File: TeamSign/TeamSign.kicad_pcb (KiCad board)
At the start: 2 copper layers, 0 parts

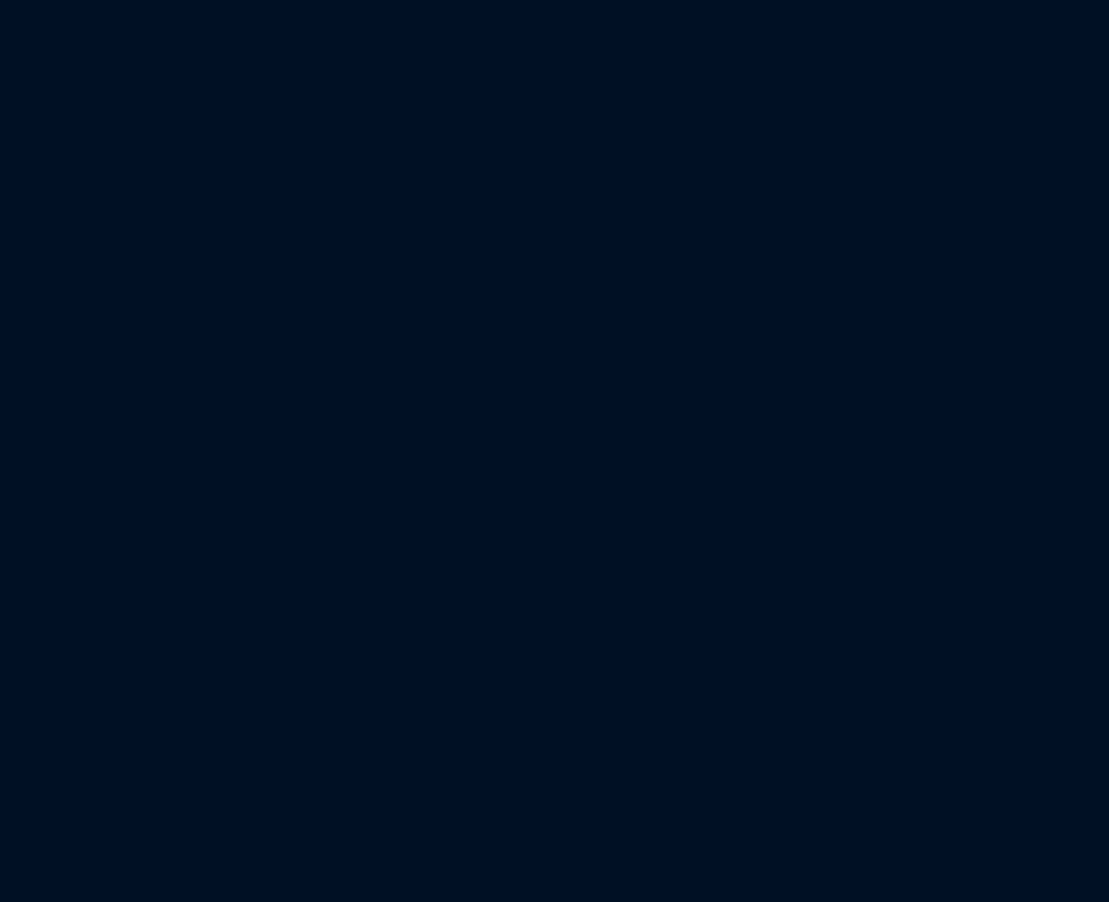
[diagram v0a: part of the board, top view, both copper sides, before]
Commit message: Add SK6812-Side-A footprint/symbol to working area, as well as swapped to a stacklight connection that has a ground pin at the end for generic 12v power use.  yay!
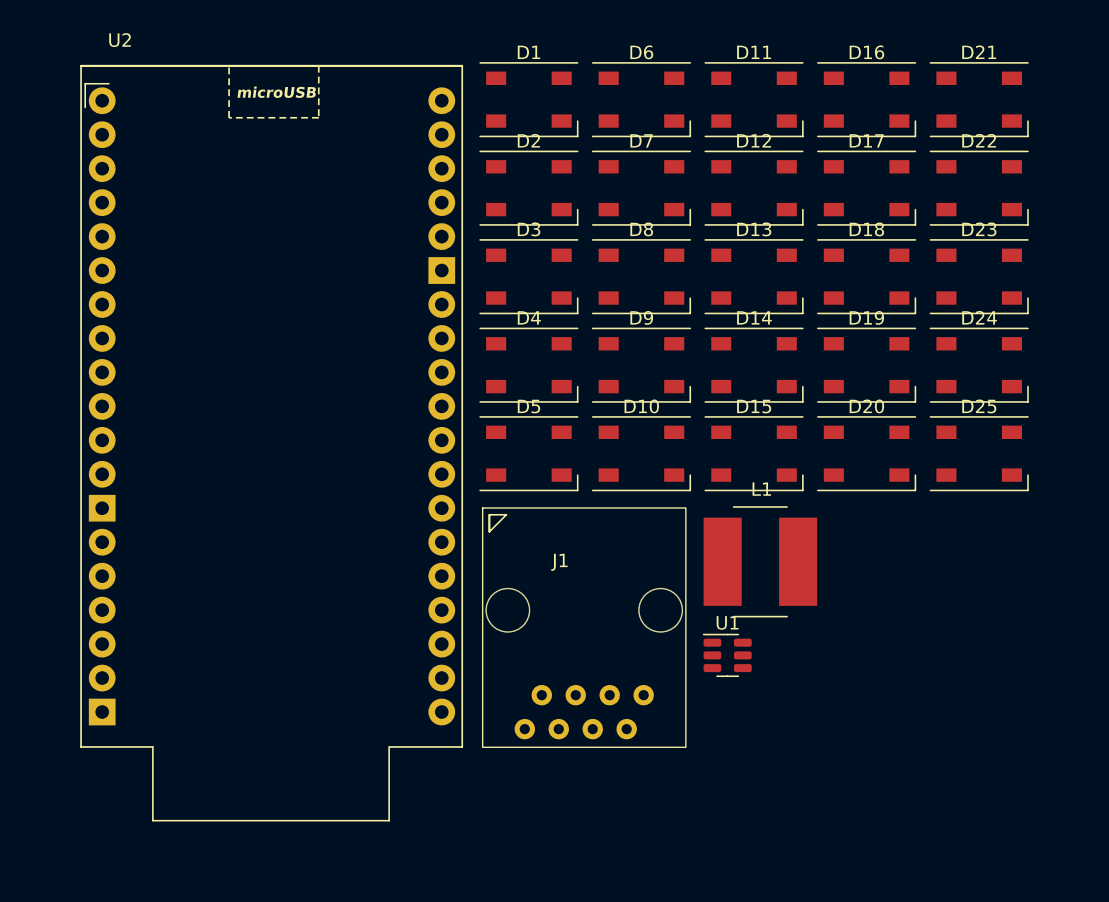
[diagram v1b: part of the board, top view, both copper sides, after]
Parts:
- added D1: SK6812, LED_SMD:LED_SK6812_PLCC4_5.0x5.0mm_P3.2mm, F.Cu at (108.5, -45.9)
- added D10: SK6812, LED_SMD:LED_SK6812_PLCC4_5.0x5.0mm_P3.2mm, F.Cu at (116.9, -19.4)
- added D11: SK6812, LED_SMD:LED_SK6812_PLCC4_5.0x5.0mm_P3.2mm, F.Cu at (125.3, -45.9)
- added D12: SK6812, LED_SMD:LED_SK6812_PLCC4_5.0x5.0mm_P3.2mm, F.Cu at (125.3, -39.3)
- added D13: SK6812, LED_SMD:LED_SK6812_PLCC4_5.0x5.0mm_P3.2mm, F.Cu at (125.3, -32.7)
- added D14: SK6812, LED_SMD:LED_SK6812_PLCC4_5.0x5.0mm_P3.2mm, F.Cu at (125.3, -26.1)
- added D15: SK6812, LED_SMD:LED_SK6812_PLCC4_5.0x5.0mm_P3.2mm, F.Cu at (125.3, -19.4)
- added D16: SK6812, LED_SMD:LED_SK6812_PLCC4_5.0x5.0mm_P3.2mm, F.Cu at (133.8, -45.9)
- added D17: SK6812, LED_SMD:LED_SK6812_PLCC4_5.0x5.0mm_P3.2mm, F.Cu at (133.8, -39.3)
- added D18: SK6812, LED_SMD:LED_SK6812_PLCC4_5.0x5.0mm_P3.2mm, F.Cu at (133.8, -32.7)
- added D19: SK6812, LED_SMD:LED_SK6812_PLCC4_5.0x5.0mm_P3.2mm, F.Cu at (133.8, -26.1)
- added D2: SK6812, LED_SMD:LED_SK6812_PLCC4_5.0x5.0mm_P3.2mm, F.Cu at (108.5, -39.3)
- added D20: SK6812, LED_SMD:LED_SK6812_PLCC4_5.0x5.0mm_P3.2mm, F.Cu at (133.8, -19.4)
- added D21: SK6812, LED_SMD:LED_SK6812_PLCC4_5.0x5.0mm_P3.2mm, F.Cu at (142.2, -45.9)
- added D22: SK6812, LED_SMD:LED_SK6812_PLCC4_5.0x5.0mm_P3.2mm, F.Cu at (142.2, -39.3)
- added D23: SK6812, LED_SMD:LED_SK6812_PLCC4_5.0x5.0mm_P3.2mm, F.Cu at (142.2, -32.7)
- added D24: SK6812, LED_SMD:LED_SK6812_PLCC4_5.0x5.0mm_P3.2mm, F.Cu at (142.2, -26.1)
- added D25: SK6812, LED_SMD:LED_SK6812_PLCC4_5.0x5.0mm_P3.2mm, F.Cu at (142.2, -19.4)
- added D3: SK6812, LED_SMD:LED_SK6812_PLCC4_5.0x5.0mm_P3.2mm, F.Cu at (108.5, -32.7)
- added D4: SK6812, LED_SMD:LED_SK6812_PLCC4_5.0x5.0mm_P3.2mm, F.Cu at (108.5, -26.1)
- added D5: SK6812, LED_SMD:LED_SK6812_PLCC4_5.0x5.0mm_P3.2mm, F.Cu at (108.5, -19.4)
- added D6: SK6812, LED_SMD:LED_SK6812_PLCC4_5.0x5.0mm_P3.2mm, F.Cu at (116.9, -45.9)
- added D7: SK6812, LED_SMD:LED_SK6812_PLCC4_5.0x5.0mm_P3.2mm, F.Cu at (116.9, -39.3)
- added D8: SK6812, LED_SMD:LED_SK6812_PLCC4_5.0x5.0mm_P3.2mm, F.Cu at (116.9, -32.7)
- added D9: SK6812, LED_SMD:LED_SK6812_PLCC4_5.0x5.0mm_P3.2mm, F.Cu at (116.9, -26.1)
- added J1: RJ45, footprints:RCH RC00139, F.Cu at (105.0, -15.4)
- added L1: 3.3uH, Inductor_SMD:L_Bourns_SRN8040TA, F.Cu at (125.8, -11.4)
- added U1: TPS563200, Package_TO_SOT_SMD:SOT-23-6, F.Cu at (123.4, -4.36)
- added U2: ESP32-Devkit_C_V4, footprints:MODULE_ESP32_DEVKIT_C_V4, F.Cu at (89.3, -23.0)
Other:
- board outline added: 14.7 x 3.2 mm

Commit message: Added subsheet for the other LEDs, still need to fix the capacitor footprint, but making solid progress it seems?  Wild!
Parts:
- added D26: SK6812-Side-A, footprints:SK6812-Side-A, F.Cu at (37.8, 56.2)
- added D27: SK6812-Side-A, footprints:SK6812-Side-A, F.Cu at (37.7, 66.3)
- added D28: SK6812-Side-A, footprints:SK6812-Side-A, F.Cu at (36.5, 78.5)
- added D29: SK6812-Side-A, footprints:SK6812-Side-A, F.Cu at (36.4, 88.9)
- added D30: SK6812-Side-A, footprints:SK6812-Side-A, F.Cu at (36.5, 99.5)
- added D31: SK6812-Side-A, footprints:SK6812-Side-A, F.Cu at (35.6, 113.6)
- added D32: SK6812-Side-A, footprints:SK6812-Side-A, F.Cu at (35.5, 125.9)
- added D33: SK6812-Side-A, footprints:SK6812-Side-A, F.Cu at (35.9, 141.9)
- added D34: SK6812, LED_SMD:LED_SK6812_PLCC4_5.0x5.0mm_P3.2mm, F.Cu at (67.2, 100.2)
- added D35: SK6812, LED_SMD:LED_SK6812_PLCC4_5.0x5.0mm_P3.2mm, F.Cu at (73.8, 100.2)
- added D36: SK6812, LED_SMD:LED_SK6812_PLCC4_5.0x5.0mm_P3.2mm, F.Cu at (80.4, 100.2)
- added D37: SK6812, LED_SMD:LED_SK6812_PLCC4_5.0x5.0mm_P3.2mm, F.Cu at (149.6, -11.7)
- added D38: SK6812, LED_SMD:LED_SK6812_PLCC4_5.0x5.0mm_P3.2mm, F.Cu at (149.6, -5.03)
- added D39: SK6812, LED_SMD:LED_SK6812_PLCC4_5.0x5.0mm_P3.2mm, F.Cu at (149.6, 1.59)
- added D40: SK6812, LED_SMD:LED_SK6812_PLCC4_5.0x5.0mm_P3.2mm, F.Cu at (149.6, 8.21)
- added D41: SK6812, LED_SMD:LED_SK6812_PLCC4_5.0x5.0mm_P3.2mm, F.Cu at (149.6, 14.8)
- added D42: SK6812, LED_SMD:LED_SK6812_PLCC4_5.0x5.0mm_P3.2mm, F.Cu at (149.6, 21.4)
- added D43: SK6812, LED_SMD:LED_SK6812_PLCC4_5.0x5.0mm_P3.2mm, F.Cu at (149.6, 28.1)
- added D44: SK6812, LED_SMD:LED_SK6812_PLCC4_5.0x5.0mm_P3.2mm, F.Cu at (158.0, -11.7)
- added D45: SK6812, LED_SMD:LED_SK6812_PLCC4_5.0x5.0mm_P3.2mm, F.Cu at (158.0, -5.03)
- added D46: SK6812, LED_SMD:LED_SK6812_PLCC4_5.0x5.0mm_P3.2mm, F.Cu at (158.0, 1.59)
- added D47: SK6812, LED_SMD:LED_SK6812_PLCC4_5.0x5.0mm_P3.2mm, F.Cu at (158.0, 8.21)
- added D48: SK6812, LED_SMD:LED_SK6812_PLCC4_5.0x5.0mm_P3.2mm, F.Cu at (158.0, 14.8)
- added D49: SK6812, LED_SMD:LED_SK6812_PLCC4_5.0x5.0mm_P3.2mm, F.Cu at (158.0, 21.4)
- added D50: SK6812, LED_SMD:LED_SK6812_PLCC4_5.0x5.0mm_P3.2mm, F.Cu at (158.0, 28.1)
- added D51: SK6812, LED_SMD:LED_SK6812_PLCC4_5.0x5.0mm_P3.2mm, F.Cu at (166.4, -11.7)
- added D52: SK6812, LED_SMD:LED_SK6812_PLCC4_5.0x5.0mm_P3.2mm, F.Cu at (166.4, -5.03)
- added D53: SK6812, LED_SMD:LED_SK6812_PLCC4_5.0x5.0mm_P3.2mm, F.Cu at (166.4, 1.59)
- added D54: SK6812, LED_SMD:LED_SK6812_PLCC4_5.0x5.0mm_P3.2mm, F.Cu at (166.4, 8.21)
- added D55: SK6812, LED_SMD:LED_SK6812_PLCC4_5.0x5.0mm_P3.2mm, F.Cu at (166.4, 14.8)
- added D56: SK6812, LED_SMD:LED_SK6812_PLCC4_5.0x5.0mm_P3.2mm, F.Cu at (166.4, 21.4)
- added D57: SK6812, LED_SMD:LED_SK6812_PLCC4_5.0x5.0mm_P3.2mm, F.Cu at (166.4, 28.1)
- added D58: SK6812, LED_SMD:LED_SK6812_PLCC4_5.0x5.0mm_P3.2mm, F.Cu at (174.8, -11.7)
- added D59: SK6812, LED_SMD:LED_SK6812_PLCC4_5.0x5.0mm_P3.2mm, F.Cu at (174.8, -5.03)
- added D60: SK6812, LED_SMD:LED_SK6812_PLCC4_5.0x5.0mm_P3.2mm, F.Cu at (174.8, 1.59)
- added D61: SK6812, LED_SMD:LED_SK6812_PLCC4_5.0x5.0mm_P3.2mm, F.Cu at (174.8, 8.21)
- added D62: SK6812, LED_SMD:LED_SK6812_PLCC4_5.0x5.0mm_P3.2mm, F.Cu at (174.8, 14.8)
- added D63: SK6812, LED_SMD:LED_SK6812_PLCC4_5.0x5.0mm_P3.2mm, F.Cu at (174.8, 21.4)
- added D64: SK6812, LED_SMD:LED_SK6812_PLCC4_5.0x5.0mm_P3.2mm, F.Cu at (174.8, 28.1)
- added D65: SK6812, LED_SMD:LED_SK6812_PLCC4_5.0x5.0mm_P3.2mm, F.Cu at (185.2, -11.7)
- added D66: SK6812, LED_SMD:LED_SK6812_PLCC4_5.0x5.0mm_P3.2mm, F.Cu at (185.2, -5.03)
- added D67: SK6812, LED_SMD:LED_SK6812_PLCC4_5.0x5.0mm_P3.2mm, F.Cu at (185.2, 1.59)
- added D68: SK6812, LED_SMD:LED_SK6812_PLCC4_5.0x5.0mm_P3.2mm, F.Cu at (185.2, 8.21)
- added D69: SK6812, LED_SMD:LED_SK6812_PLCC4_5.0x5.0mm_P3.2mm, F.Cu at (185.2, 14.8)
- added D70: SK6812, LED_SMD:LED_SK6812_PLCC4_5.0x5.0mm_P3.2mm, F.Cu at (185.2, 21.4)
- added D71: SK6812, LED_SMD:LED_SK6812_PLCC4_5.0x5.0mm_P3.2mm, F.Cu at (185.2, 28.1)
- added D72: SK6812, LED_SMD:LED_SK6812_PLCC4_5.0x5.0mm_P3.2mm, F.Cu at (193.7, -11.7)
- added D73: SK6812, LED_SMD:LED_SK6812_PLCC4_5.0x5.0mm_P3.2mm, F.Cu at (193.7, -5.03)
- added D74: SK6812, LED_SMD:LED_SK6812_PLCC4_5.0x5.0mm_P3.2mm, F.Cu at (193.7, 1.59)
- added D75: SK6812, LED_SMD:LED_SK6812_PLCC4_5.0x5.0mm_P3.2mm, F.Cu at (193.7, 8.21)
- added D76: SK6812, LED_SMD:LED_SK6812_PLCC4_5.0x5.0mm_P3.2mm, F.Cu at (193.7, 14.8)
- added D77: SK6812, LED_SMD:LED_SK6812_PLCC4_5.0x5.0mm_P3.2mm, F.Cu at (193.7, 21.4)
- added D78: SK6812, LED_SMD:LED_SK6812_PLCC4_5.0x5.0mm_P3.2mm, F.Cu at (193.7, 28.1)
- added D79: SK6812, LED_SMD:LED_SK6812_PLCC4_5.0x5.0mm_P3.2mm, F.Cu at (202.1, -11.7)
- added D80: SK6812, LED_SMD:LED_SK6812_PLCC4_5.0x5.0mm_P3.2mm, F.Cu at (202.1, -5.03)
- added D81: SK6812, LED_SMD:LED_SK6812_PLCC4_5.0x5.0mm_P3.2mm, F.Cu at (202.1, 1.59)
- added D82: SK6812, LED_SMD:LED_SK6812_PLCC4_5.0x5.0mm_P3.2mm, F.Cu at (202.1, 8.21)
- added D83: SK6812, LED_SMD:LED_SK6812_PLCC4_5.0x5.0mm_P3.2mm, F.Cu at (202.1, 14.8)
- added D84: SK6812, LED_SMD:LED_SK6812_PLCC4_5.0x5.0mm_P3.2mm, F.Cu at (202.1, 21.4)
- added D85: SK6812, LED_SMD:LED_SK6812_PLCC4_5.0x5.0mm_P3.2mm, F.Cu at (202.1, 28.1)
- added D86: SK6812, LED_SMD:LED_SK6812_PLCC4_5.0x5.0mm_P3.2mm, F.Cu at (210.5, -11.7)
- added D87: SK6812, LED_SMD:LED_SK6812_PLCC4_5.0x5.0mm_P3.2mm, F.Cu at (210.5, -5.03)
- added D88: SK6812, LED_SMD:LED_SK6812_PLCC4_5.0x5.0mm_P3.2mm, F.Cu at (210.5, 1.59)
- added D89: SK6812, LED_SMD:LED_SK6812_PLCC4_5.0x5.0mm_P3.2mm, F.Cu at (210.5, 8.21)
- added D90: SK6812, LED_SMD:LED_SK6812_PLCC4_5.0x5.0mm_P3.2mm, F.Cu at (210.5, 14.8)
- added D91: SK6812, LED_SMD:LED_SK6812_PLCC4_5.0x5.0mm_P3.2mm, F.Cu at (210.5, 21.4)
- added D92: SK6812, LED_SMD:LED_SK6812_PLCC4_5.0x5.0mm_P3.2mm, F.Cu at (210.5, 28.1)
- J1, U2: moved to B.Cu
- moved D16 198.2 mm to (82.0, 145.4), turned to 90 degrees
- moved D13 192.0 mm to (54.3, 145.6), turned to 90 degrees
- moved D14 182.6 mm to (63.3, 145.6), turned to 90 degrees
- moved D12 178.3 mm to (98.5, 136.9)
- moved D17 176.7 mm to (45.2, 113.6)
- moved D18 176.7 mm to (45.2, 120.2)
- moved D19 176.7 mm to (45.2, 126.8)
- moved D20 176.7 mm to (45.2, 133.4)
- moved D11 176.0 mm to (98.5, 128.0)
- moved D15 173.3 mm to (72.2, 145.5), turned to 90 degrees
- moved D21 149.4 mm to (45.6, 68.0)
- moved D22 149.4 mm to (45.6, 74.7)
- moved D23 149.4 mm to (45.6, 81.3)
- moved D24 149.4 mm to (45.6, 87.9)
- moved D25 145.8 mm to (58.8, 100.2), turned to 90 degrees
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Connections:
- D1 pad 2: /sk_input -> /LED Array 1/sk_pin1
- D10 pad 3: +3V3 -> +5V
- D11 pad 2: Net-(D10-DOUT) -> Net-(D11-DIN)
- D12 pad 2: Net-(D11-DOUT) -> Net-(D10-DOUT)
- D12 pad 3: +3V3 -> +5V
- D12 pad 4: /sk_pin1 -> Net-(D12-DOUT)
- D13 pad 1: Net-(D13-VSS) -> GND
- D13 pad 2: /sk_pin1 -> Net-(D11-DOUT)
- D13 pad 3: Net-(D13-VDD) -> +3V3
- D14 pad 1: Net-(D13-VSS) -> GND
- D14 pad 2: Net-(D13-DOUT) -> Net-(D12-DOUT)
- D14 pad 3: Net-(D13-VDD) -> +5V
- D15 pad 1: Net-(D13-VSS) -> GND
- D15 pad 2: Net-(D14-DOUT) -> Net-(D13-DOUT)
- D15 pad 3: Net-(D13-VDD) -> +3V3
- D16 pad 1: Net-(D13-VSS) -> GND
- D16 pad 2: Net-(D15-DOUT) -> Net-(D14-DOUT)
- D16 pad 3: Net-(D13-VDD) -> +5V
- D17 pad 1: Net-(D13-VSS) -> GND
- D17 pad 2: Net-(D16-DOUT) -> Net-(D15-DOUT)
- D17 pad 3: Net-(D13-VDD) -> +3V3
- D18 pad 1: Net-(D13-VSS) -> GND
- D18 pad 2: Net-(D17-DOUT) -> Net-(D16-DOUT)
- D18 pad 3: Net-(D13-VDD) -> +5V
- D19 pad 1: Net-(D13-VSS) -> GND
- D19 pad 2: Net-(D18-DOUT) -> Net-(D17-DOUT)
- D19 pad 3: Net-(D13-VDD) -> +3V3
- D2 pad 2: Net-(D1-DOUT) -> /sk_input
- D2 pad 3: +3V3 -> +5V
- D20 pad 1: Net-(D13-VSS) -> GND
- D20 pad 2: Net-(D19-DOUT) -> Net-(D18-DOUT)
- D20 pad 3: Net-(D13-VDD) -> +5V
- D21 pad 1: Net-(D13-VSS) -> GND
- D21 pad 2: Net-(D20-DOUT) -> Net-(D19-DOUT)
- D21 pad 3: Net-(D13-VDD) -> +3V3
- D22 pad 1: Net-(D13-VSS) -> GND
- D22 pad 2: Net-(D21-DOUT) -> Net-(D20-DOUT)
- D22 pad 3: Net-(D13-VDD) -> +5V
- D23 pad 1: Net-(D13-VSS) -> GND
- D23 pad 2: Net-(D22-DOUT) -> Net-(D21-DOUT)
- D23 pad 3: Net-(D13-VDD) -> +3V3
- D24 pad 1: Net-(D13-VSS) -> GND
- D24 pad 2: Net-(D23-DOUT) -> Net-(D22-DOUT)
- D24 pad 3: Net-(D13-VDD) -> +5V
- D24 pad 4: Net-(D24-DOUT) -> /LED Array 1/sk_pin1
- D25 pad 1: Net-(D13-VSS) -> GND
- D25 pad 2: Net-(D24-DOUT) -> Net-(D23-DOUT)
- D25 pad 3: Net-(D13-VDD) -> +3V3
- D25 pad 4: unconnected-(D25-DOUT-Pad4) -> /LED Array 1/sk_pin2
- D3 pad 2: Net-(D2-DOUT) -> Net-(D1-DOUT)
- D4 pad 2: Net-(D3-DOUT) -> Net-(D2-DOUT)
- D4 pad 3: +3V3 -> +5V
- D5 pad 2: Net-(D4-DOUT) -> Net-(D3-DOUT)
- D6 pad 2: Net-(D5-DOUT) -> Net-(D4-DOUT)
- D6 pad 3: +3V3 -> +5V
- D7 pad 2: Net-(D6-DOUT) -> Net-(D5-DOUT)
- D8 pad 2: Net-(D7-DOUT) -> Net-(D6-DOUT)
- D8 pad 3: +3V3 -> +5V
- D8 pad 4: Net-(D8-DOUT) -> Net-(D10-DIN)
- D9 pad 2: Net-(D8-DOUT) -> Net-(D7-DOUT)
- D9 pad 4: Net-(D10-DIN) -> Net-(D11-DIN)
- L1 pad 2: +3V3 -> +5V
- U2 pad 20: +3V3 -> unconnected-(U2-3.3v-Pad20)
- U2 pad 27: unconnected-(U2-RTC_GPIO8/Xtal32N/Touch8/ADC1_5/GPIO33-Pad27) -> /stacklight_out
- U2 pad 38: unconnected-(U2-5V-Pad38) -> +5V
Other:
- board size 14.7 x 3.2 mm -> 235.8 x 134.4 mm

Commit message: Add PEM nut footprint starter to library, also did small tweaks to BOM and updated symbols to include the barrel jack antics.  Yay!
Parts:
- added C1: 10uF, Capacitor_SMD:C_1206_3216Metric_Pad1.33x1.80mm_HandSolder, F.Cu at (170.2, 24.6)
- added C2: 100nF, Capacitor_SMD:C_1206_3216Metric_Pad1.33x1.80mm_HandSolder, F.Cu at (170.2, 27.9)
- added C3: 22uF, Capacitor_SMD:CP_Elec_5x5.4, F.Cu at (153.7, 27.1)
- added C96: 22uF, Capacitor_SMD:CP_Elec_5x5.4, F.Cu at (153.7, 33.9)
- added C97: 10uF, Capacitor_SMD:C_1206_3216Metric_Pad1.33x1.80mm_HandSolder, F.Cu at (170.2, 31.2)
- added J2: Barrel_Jack_MountingPin, Connector_BarrelJack:BarrelJack_Horizontal, F.Cu at (138.0, 33.2)
- added R1: 54.9kΩ, Resistor_SMD:R_0805_2012Metric_Pad1.20x1.40mm_HandSolder, F.Cu at (160.5, 25.1)
- added R2: 10kΩ, Resistor_SMD:R_0805_2012Metric_Pad1.20x1.40mm_HandSolder, F.Cu at (160.5, 28.1)
- added R3: 10kΩ, Resistor_SMD:R_0805_2012Metric_Pad1.20x1.40mm_HandSolder, F.Cu at (160.5, 31.0)
- moved D79 158.4 mm to (226.2, 144.9), turned to -90 degrees
- moved D51 157.9 mm to (148.2, 145.2), turned to -90 degrees
- moved D52 152.3 mm to (141.5, 145.2), turned to -90 degrees
- moved D80 151.0 mm to (219.5, 144.9), turned to -90 degrees
- moved D53 138.9 mm to (125.0, 134.2), turned to 180 degrees
- moved D73 134.9 mm to (257.7, 113.7)
- moved D74 134.9 mm to (257.7, 120.3)
- moved D75 134.9 mm to (257.7, 126.9)
- moved D76 134.9 mm to (257.7, 133.5)
- moved D81 132.4 mm to (205.3, 133.9), turned to 180 degrees
- moved D77 131.8 mm to (238.9, 145.2), turned to -90 degrees
- moved D54 126.3 mm to (125.0, 127.5), turned to 180 degrees
- moved D49 123.8 mm to (161.2, 145.2), turned to -90 degrees
- moved D78 123.3 mm to (232.3, 145.2), turned to -90 degrees
- moved D46 120.5 mm to (177.4, 120.5)
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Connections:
- D1 pad 2: /LED Array 1/sk_pin1 -> /sk_input
- D1 pad 3: +3V3 -> +5V
- D11 pad 2: Net-(D11-DIN) -> Net-(D10-DOUT)
- D11 pad 3: +3V3 -> +5V
- D12 pad 2: Net-(D10-DOUT) -> Net-(D11-DOUT)
- D12 pad 4: Net-(D12-DOUT) -> /LED Array 1/sk_pin1
- D13 pad 2: Net-(D11-DOUT) -> /LED Array 1/sk_pin1
- D14 pad 2: Net-(D12-DOUT) -> Net-(D13-DOUT)
- D14 pad 3: +5V -> +3V3
- D15 pad 2: Net-(D13-DOUT) -> Net-(D14-DOUT)
- D16 pad 2: Net-(D14-DOUT) -> Net-(D15-DOUT)
- D16 pad 3: +5V -> +3V3
- D17 pad 2: Net-(D15-DOUT) -> Net-(D16-DOUT)
- D18 pad 2: Net-(D16-DOUT) -> Net-(D17-DOUT)
- D18 pad 3: +5V -> +3V3
- D19 pad 2: Net-(D17-DOUT) -> Net-(D18-DOUT)
- D2 pad 2: /sk_input -> Net-(D1-DOUT)
- D20 pad 2: Net-(D18-DOUT) -> Net-(D19-DOUT)
- D20 pad 3: +5V -> +3V3
- D21 pad 2: Net-(D19-DOUT) -> Net-(D20-DOUT)
- D22 pad 2: Net-(D20-DOUT) -> Net-(D21-DOUT)
- D22 pad 3: +5V -> +3V3
- D23 pad 2: Net-(D21-DOUT) -> Net-(D22-DOUT)
- D24 pad 2: Net-(D22-DOUT) -> Net-(D23-DOUT)
- D24 pad 3: +5V -> +3V3
- D24 pad 4: /LED Array 1/sk_pin1 -> Net-(D24-DOUT)
- D25 pad 2: Net-(D23-DOUT) -> Net-(D24-DOUT)
- D3 pad 2: Net-(D1-DOUT) -> Net-(D2-DOUT)
- D3 pad 3: +3V3 -> +5V
- D4 pad 2: Net-(D2-DOUT) -> Net-(D3-DOUT)
- D5 pad 2: Net-(D3-DOUT) -> Net-(D4-DOUT)
- D5 pad 3: +3V3 -> +5V
- D6 pad 2: Net-(D4-DOUT) -> Net-(D5-DOUT)
- D7 pad 2: Net-(D5-DOUT) -> Net-(D6-DOUT)
- D7 pad 3: +3V3 -> +5V
- D8 pad 2: Net-(D6-DOUT) -> Net-(D7-DOUT)
- D8 pad 4: Net-(D10-DIN) -> Net-(D8-DOUT)
- D9 pad 2: Net-(D7-DOUT) -> Net-(D8-DOUT)
- D9 pad 3: +3V3 -> +5V
- D9 pad 4: Net-(D11-DIN) -> Net-(D10-DIN)
- U1 pad 5: unconnected-(U1-EN-Pad5) -> Net-(U1-EN)
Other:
- board size 235.8 x 134.4 mm -> 259.2 x 139.8 mm
